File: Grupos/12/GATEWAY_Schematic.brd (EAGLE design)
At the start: 70.5 x 59.4 mm, 13 parts

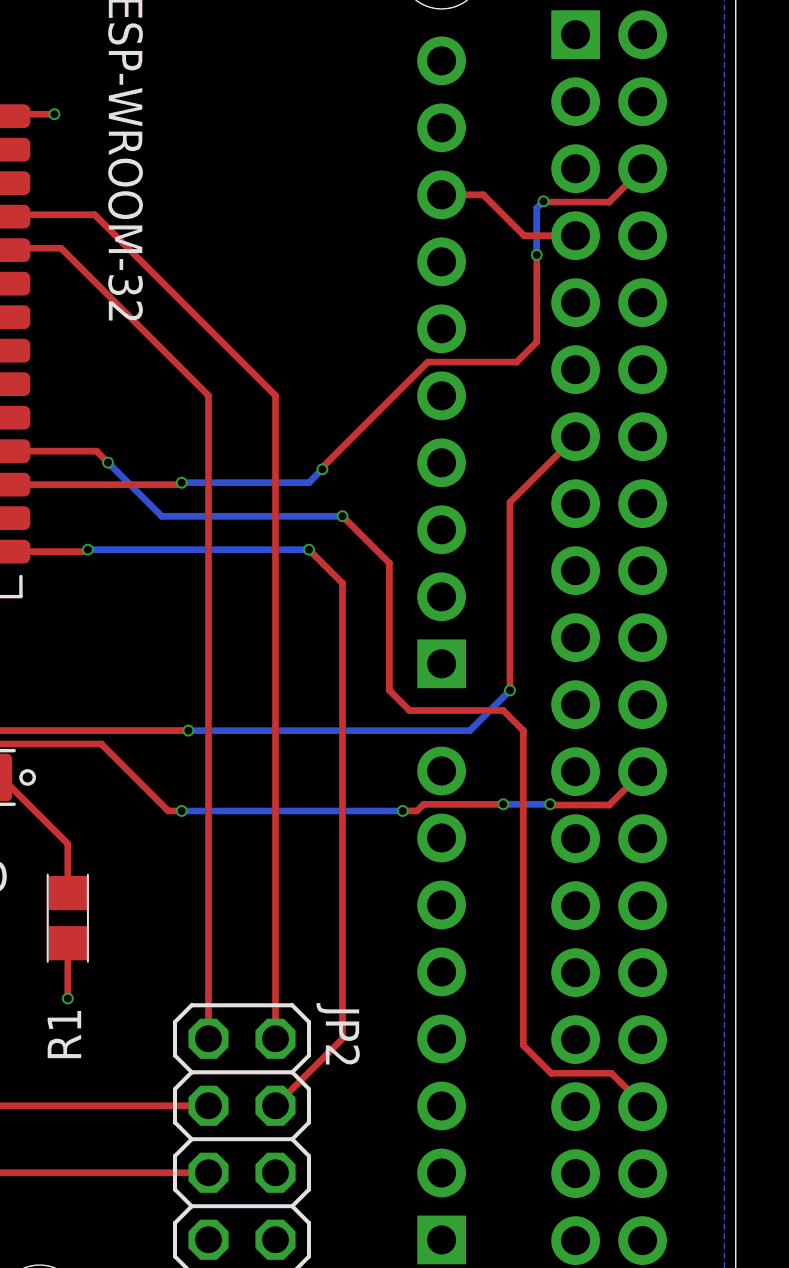
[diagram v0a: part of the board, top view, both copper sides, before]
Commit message: Swap RTS/CTS and RX/TX
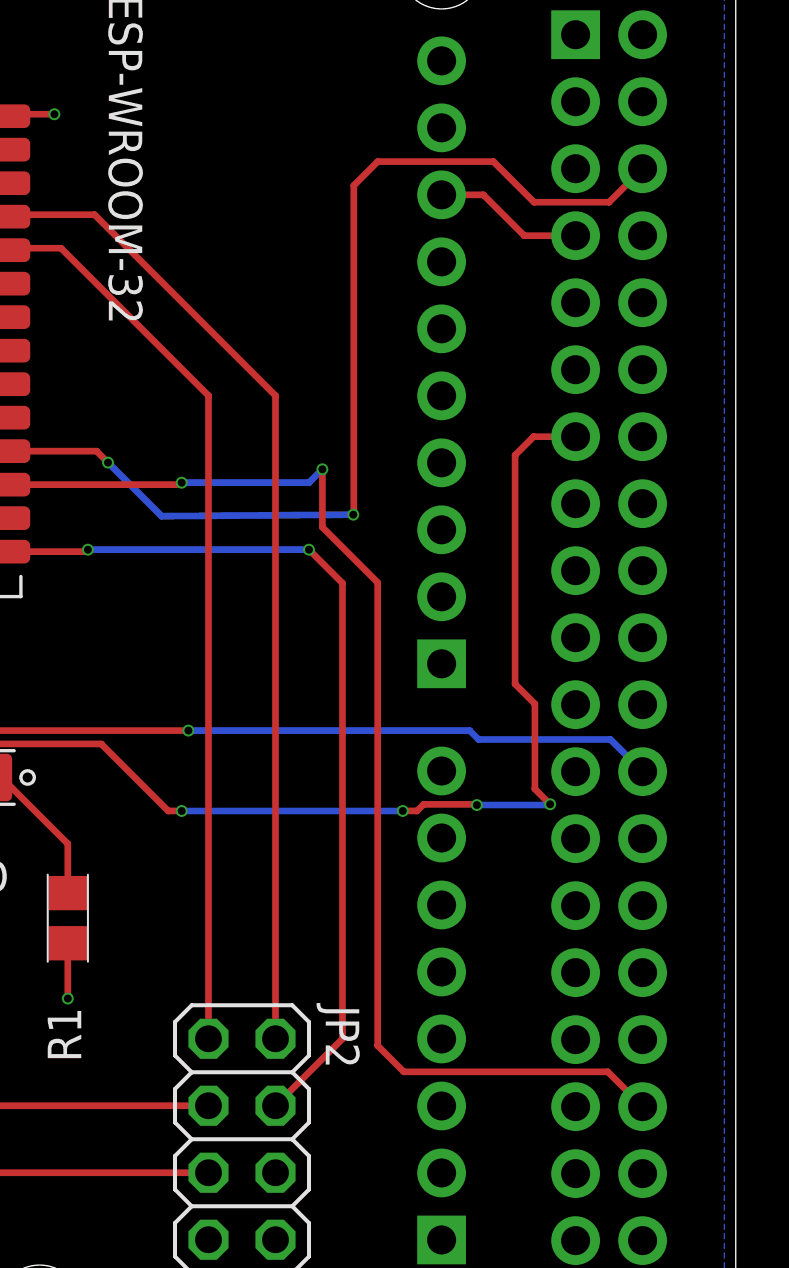
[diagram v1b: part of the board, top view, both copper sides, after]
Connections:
- net CTS: now also M1.CN10-24; no longer M1.CN10-13
- net RTS: now also M1.CN10-13; no longer M1.CN10-24
- net RX: now also M1.CN10-34; no longer M1.CN10-6
- net TX: now also M1.CN10-6; no longer M1.CN10-34
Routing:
- net RX: track 32.0 -> 45.9 mm, vias 4 -> 2
- net RTS: track 50.4 -> 62.8 mm
- net CTS: track 38.8 -> 33.2 mm, vias 2 -> 1
- net TX: track 44.1 -> 39.0 mm
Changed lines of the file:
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@@
 <drawing>
 <settings>
-<setting alwaysvectorfont="no"/>
+<setting alwaysvectorfont="yes"/>
 <setting verticaltext="up"/>
 </settings>
@@
 </signal>
 <signal name="TX">
-<contactref element="M1" pad="CN10-34"/>
 <contactref element="ESP-WROOM-32" pad="28"/>
 <wire x1="43.04" y1="35.232" x2="46.302" y2="35.232" width="0.254" layer="1"/>
@@
 <via x="46.736" y="34.798" extent="1-16" drill="0.3"/>
 <wire x1="46.736" y1="34.798" x2="48.768" y2="32.766" width="0.254" layer="16"/>
-<wire x1="48.768" y1="32.766" x2="55.626" y2="32.766" width="0.254" layer="16"/>
-<via x="55.626" y="32.766" extent="1-16" drill="0.3"/>
-<wire x1="55.626" y1="32.766" x2="57.404" y2="30.988" width="0.254" layer="1"/>
-<wire x1="57.404" y1="30.988" x2="57.404" y2="26.162" width="0.254" layer="1"/>
-<wire x1="57.404" y1="26.162" x2="58.166" y2="25.4" width="0.254" layer="1"/>
-<wire x1="58.166" y1="25.4" x2="61.722" y2="25.4" width="0.254" layer="1"/>
-<wire x1="61.722" y1="25.4" x2="62.484" y2="24.638" width="0.254" layer="1"/>
-<wire x1="62.484" y1="24.638" x2="62.484" y2="12.7" width="0.254" layer="1"/>
-<wire x1="62.484" y1="12.7" x2="63.54" y2="11.644" width="0.254" layer="1"/>
-<wire x1="63.54" y1="11.644" x2="65.826" y2="11.644" width="0.254" layer="1"/>
-<wire x1="65.826" y1="11.644" x2="67.004" y2="10.466" width="0.254" layer="1"/>
-<wire x1="67.004" y1="10.466" x2="67.004" y2="10.38100625" width="0.254" layer="1"/>
+<wire x1="48.768" y1="32.766" x2="56.036" y2="32.824" width="0.254" layer="16"/>
+<via x="56.036" y="32.824" extent="1-16" drill="0.3"/>
+<contactref element="M1" pad="CN10-6"/>
+<wire x1="67.004" y1="45.94100625" x2="65.73299375" y2="44.67" width="0.254" layer="1"/>
+<wire x1="56.056" y1="45.306" x2="56.056" y2="32.824" width="0.254" layer="1"/>
+<wire x1="56.036" y1="32.824" x2="56.056" y2="32.824" width="0.254" layer="1"/>
+<wire x1="65.73299375" y1="44.67" x2="62.89" y2="44.67" width="0.254" layer="1"/>
+<wire x1="62.89" y1="44.67" x2="61.35" y2="46.21" width="0.254" layer="1"/>
+<wire x1="61.35" y1="46.21" x2="56.96" y2="46.21" width="0.254" layer="1"/>
+<wire x1="56.96" y1="46.21" x2="56.056" y2="45.306" width="0.254" layer="1"/>
 </signal>
 <signal name="RX">
-<contactref element="M1" pad="CN10-6"/>
 <contactref element="ESP-WROOM-32" pad="27"/>
 <wire x1="43.04" y1="33.962" x2="49.456" y2="33.962" width="0.254" layer="1"/>
@@
 <wire x1="54.356" y1="34.036" x2="54.864" y2="34.544" width="0.254" layer="16"/>
 <via x="54.864" y="34.544" extent="1-16" drill="0.3"/>
-<wire x1="58.858" y1="38.608" x2="54.864" y2="34.614" width="0.254" layer="1"/>
 <wire x1="54.864" y1="34.544" x2="54.864" y2="34.614" width="0.254" layer="1"/>
-<wire x1="58.858" y1="38.608" x2="62.23" y2="38.608" width="0.254" layer="1"/>
-<wire x1="62.23" y1="38.608" x2="62.992" y2="39.37" width="0.254" layer="1"/>
-<wire x1="62.992" y1="39.37" x2="62.992" y2="42.672" width="0.254" layer="1"/>
-<via x="62.992" y="42.672" extent="1-16" drill="0.3"/>
-<wire x1="62.992" y1="42.672" x2="62.992" y2="44.45" width="0.254" layer="16"/>
-<wire x1="62.992" y1="44.45" x2="63.246" y2="44.704" width="0.254" layer="16"/>
-<via x="63.246" y="44.704" extent="1-16" drill="0.3"/>
-<wire x1="65.73699375" y1="44.674" x2="63.276" y2="44.674" width="0.254" layer="1"/>
-<wire x1="63.246" y1="44.704" x2="63.276" y2="44.674" width="0.254" layer="1"/>
-<wire x1="65.73699375" y1="44.674" x2="67.004" y2="45.94100625" width="0.254" layer="1"/>
+<contactref element="M1" pad="CN10-34"/>
+<wire x1="54.864" y1="34.544" x2="54.864" y2="32.346" width="0.254" layer="1"/>
+<wire x1="65.68500625" y1="11.7" x2="67.004" y2="10.38100625" width="0.254" layer="1"/>
+<wire x1="54.864" y1="32.346" x2="56.96" y2="30.25" width="0.254" layer="1"/>
+<wire x1="56.96" y1="30.25" x2="56.96" y2="12.69" width="0.254" layer="1"/>
+<wire x1="56.96" y1="12.69" x2="57.95" y2="11.7" width="0.254" layer="1"/>
+<wire x1="57.95" y1="11.7" x2="65.68500625" y2="11.7" width="0.254" layer="1"/>
 </signal>
 <signal name="CTS">
-<contactref element="M1" pad="CN10-13"/>
 <contactref element="ESP-WROOM-32" pad="23"/>
 <wire x1="38.74" y1="30.172" x2="38.74" y2="26.792" width="0.254" layer="1"/>
@@
 <via x="49.784" y="24.638" extent="1-16" drill="0.3"/>
 <wire x1="49.784" y1="24.638" x2="60.452" y2="24.638" width="0.254" layer="16"/>
-<wire x1="60.452" y1="24.638" x2="61.976" y2="26.162" width="0.254" layer="16"/>
-<via x="61.976" y="26.162" extent="1-16" drill="0.3"/>
-<wire x1="61.976" y1="26.162" x2="61.976" y2="33.29300625" width="0.254" layer="1"/>
-<wire x1="61.976" y1="33.29300625" x2="64.464" y2="35.78100625" width="0.254" layer="1"/>
 <wire x1="38.74" y1="26.792" x2="40.894" y2="24.638" width="0.254" layer="1"/>
+<contactref element="M1" pad="CN10-24"/>
+<wire x1="60.452" y1="24.638" x2="60.79" y2="24.3" width="0.254" layer="16"/>
+<wire x1="65.78500625" y1="24.3" x2="67.004" y2="23.08100625" width="0.254" layer="16"/>
+<wire x1="60.79" y1="24.3" x2="65.78500625" y2="24.3" width="0.254" layer="16"/>
 </signal>
 <signal name="RTS">
-<contactref element="M1" pad="CN10-24"/>
 <contactref element="ESP-WROOM-32" pad="13"/>
 <wire x1="25.54" y1="32.692" x2="24.564" y2="32.692" width="0.254" layer="1"/>
@@
 <wire x1="49.53" y1="21.59" x2="57.912" y2="21.59" width="0.254" layer="16"/>
 <via x="57.912" y="21.59" extent="1-16" drill="0.3"/>
-<via x="61.722" y="21.844" extent="1-16" drill="0.3"/>
+<via x="60.722" y="21.814" extent="1-16" drill="0.3"/>
 <wire x1="57.912" y1="21.59" x2="58.45071875" y2="21.59" width="0.254" layer="1"/>
 <wire x1="58.45071875" y1="21.59" x2="58.70111875" y2="21.8404" width="0.254" layer="1"/>
-<wire x1="61.722" y1="21.844" x2="61.7184" y2="21.8404" width="0.254" layer="1"/>
-<wire x1="61.7184" y1="21.8404" x2="58.70111875" y2="21.8404" width="0.254" layer="1"/>
-<wire x1="61.722" y1="21.844" x2="63.5" y2="21.844" width="0.254" layer="16"/>
+<wire x1="60.722" y1="21.814" x2="60.6956" y2="21.8404" width="0.254" layer="1"/>
+<wire x1="60.6956" y1="21.8404" x2="58.70111875" y2="21.8404" width="0.254" layer="1"/>
+<wire x1="63.47" y1="21.814" x2="60.722" y2="21.814" width="0.254" layer="16"/>
+<wire x1="63.47" y1="21.814" x2="63.5" y2="21.844" width="0.254" layer="16"/>
 <via x="63.5" y="21.844" extent="1-16" drill="0.3"/>
-<wire x1="65.73699375" y1="21.814" x2="63.53" y2="21.814" width="0.254" layer="1"/>
-<wire x1="63.5" y1="21.844" x2="63.53" y2="21.814" width="0.254" layer="1"/>
-<wire x1="65.73699375" y1="21.814" x2="67.004" y2="23.08100625" width="0.254" layer="1"/>
+<contactref element="M1" pad="CN10-13"/>
+<wire x1="63.5" y1="21.844" x2="62.92" y2="22.424" width="0.254" layer="1"/>
+<wire x1="62.87100625" y1="35.78100625" x2="64.464" y2="35.78100625" width="0.254" layer="1"/>
+<wire x1="62.92" y1="22.424" x2="62.92" y2="25.65" width="0.254" layer="1"/>
+<wire x1="62.92" y1="25.65" x2="62.17" y2="26.4" width="0.254" layer="1"/>
+<wire x1="62.17" y1="26.4" x2="62.17" y2="35.08" width="0.254" layer="1"/>
+<wire x1="62.17" y1="35.08" x2="62.87100625" y2="35.78100625" width="0.254" layer="1"/>
 </signal>
 <signal name="GPIO">
@@
 <mfgpreviewcolor name="substratecolor" color="0xFF786E46"/>
 </mfgpreviewcolors>
+<errors>
+</errors>
 </board>
 </drawing>
